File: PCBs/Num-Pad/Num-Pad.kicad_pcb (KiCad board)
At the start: 4 copper layers, 80 x 80 mm, 29 parts, among them J1 Male_Pogo_Connector_01x05, J2 Male_Pogo_Connector_01x05, J3 Male_Pogo_Connector_01x05, J4 Male_Pogo_Connector_01x05, SW1 SW_Push_45deg, SW10 SW_Push_45deg, SW11 SW_Push_45deg, SW12 SW_Push_45deg, SW2 SW_Push_45deg, SW3 SW_Push_45deg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

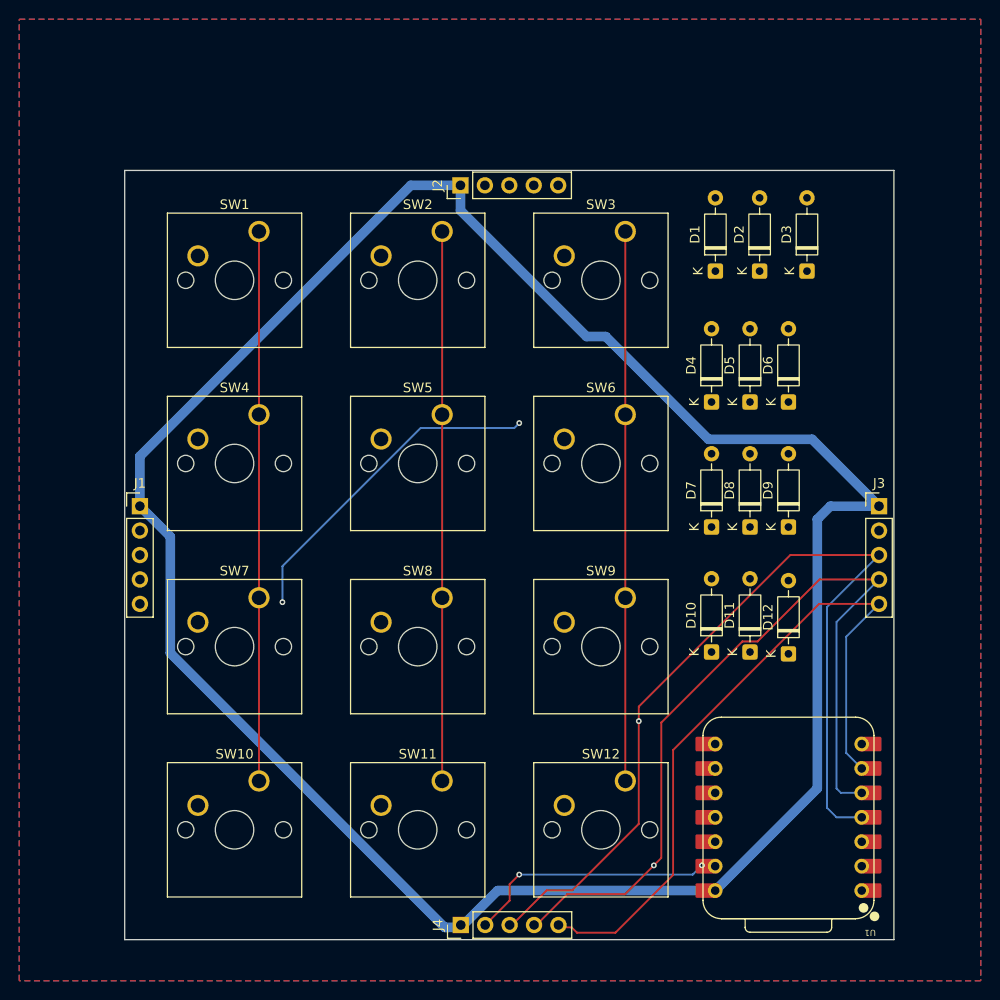
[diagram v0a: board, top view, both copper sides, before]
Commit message: Refactor I2C module handling and update PCB files
Major refactor of I2C communication between the main board and modules: unified pin naming, improved interrupt and keymap handling, and enhanced display logic in the main firmware. Updated PCB project files, added new production outputs (BOM, netlist, positions), and removed obsolete zipped PCB files. Hardware pin assignments and I2C protocol logic were aligned across modules for consistency and reliability.
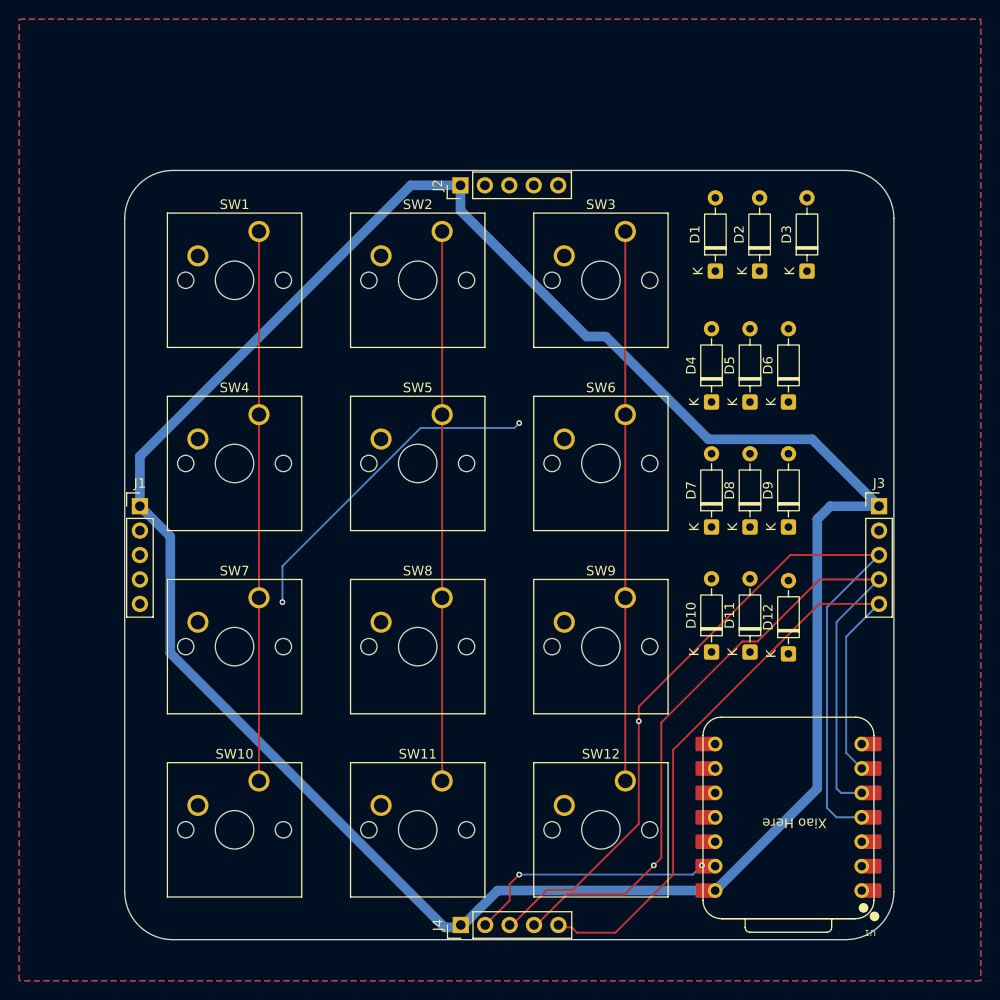
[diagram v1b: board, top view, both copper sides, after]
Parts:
- added G***: LOGO, LOGO, B.Cu at (149.0, 101.0)
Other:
- outline, holes or cut-outs redrawn
- board text added: "BeanPad NumPad Ginobeano V1"
- board text added: "Xiao Here"
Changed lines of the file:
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@@
 		)
 	)
-	(gr_rect
-		(start 90.96875 45.725)
-		(end 170.96875 125.725)
-		(stroke
-			(width 0.05)
-			(type default)
-		)
-		(fill no)
-		(layer "Edge.Cuts")
+	(footprint "LOGO"
+		(layer "B.Cu")
+		(at 149 101 -90)
+		(property "Reference" "G***"
+			(at 0 0 90)
+			(layer "B.SilkS")
+			(effects
+				(font
+					(size 1.5 1.5)
+					(thickness 0.3)
+				)
+				(justify mirror)
+			)
+		)
+		(property "Value" "LOGO"
+			(at 0.75 0 90)
+			(layer "B.SilkS")
+			(hide yes)
+			(effects
+				(font
+					(size 1.5 1.5)
+					(thickness 0.3)
+				)
+				(justify mirror)
+			)
+		)
+		(property "Datasheet" ""
+			(at 0 0 90)
+			(layer "B.Fab")
+			(hide yes)
+			(effects
+				(font
+					(size 1.27 1.27)
+					(thickness 0.15)
+				)
+				(justify mirror)
+			)
+		)
+		(property "Description" ""
+			(at 0 0 90)
+			(layer "B.Fab")
+			(hide yes)
+			(effects
+				(font
+					(size 1.27 1.27)
+					(thickness 0.15)
+				)
+				(justify mirror)
+			)
+		)
+		(attr board_only exclude_from_pos_files exclude_from_bom)
+		(fp_poly
+			(pts
+				(xy 11.286345 21.165835) (xy 12.614508 20.862313) (xy 13.919706 20.3992) (xy 14.604999 20.0848)
+				(xy 15.671747 19.467551) (xy 16.694462 18.70588) (xy 17.649618 17.823455) (xy 18.513686 16.84394)
+				(xy 19.26314 15.791001) (xy 19.781561 14.877713) (xy 20.051012 14.275829) (xy 20.312608 13.571256)
+				(xy 20.544686 12.830073) (xy 20.725577 12.11836) (xy 20.787079 11.811001) (xy 20.871597 11.202371)
+				(xy 20.933474 10.478661) (xy 20.971129 9.692812) (xy 20.98298 8.897763) (xy 20.967446 8.146453)
+				(xy 20.922945 7.491822) (xy 20.917637 7.441041) (xy 20.596928 5.255138) (xy 20.11204 3.090605) (xy 19.467729 0.957159)
+				(xy 18.668747 -1.135483) (xy 17.71985 -3.177601) (xy 16.62579 -5.159477) (xy 15.391323 -7.071394)
+				(xy 14.021202 -8.903632) (xy 12.520181 -10.646475) (xy 11.602011 -11.602011) (xy 9.89968 -13.193824)
+				(xy 8.119111 -14.640138) (xy 6.245781 -15.951425) (xy 4.265168 -17.138155) (xy 2.996851 -17.805998)
+				(xy 1.454155 -18.524908) (xy -0.131462 -19.161046) (xy -1.739936 -19.70995) (xy -3.351204 -20.167154)
+				(xy -4.945202 -20.528196) (xy -6.501868 -20.788612) (xy -8.001136 -20.943937) (xy -9.422944 -20.989707)
+				(xy -10.747228 -20.92146) (xy -10.922001 -20.902747) (xy -12.2785 -20.665051) (xy -13.577246 -20.274384)
+				(xy -14.808226 -19.740238) (xy -15.961426 -19.072106) (xy -17.026832 -18.279483) (xy -17.994431 -17.37186)
+				(xy -18.854209 -16.358731) (xy -19.596153 -15.249589) (xy -20.210248 -14.053927) (xy -20.686481 -12.781238)
+				(xy -21.014839 -11.441015) (xy -21.03754 -11.313075) (xy -21.109334 -10.73445) (xy -21.151212 -10.04694)
+				(xy -21.163235 -9.307275) (xy -21.145461 -8.572184) (xy -21.097948 -7.898397) (xy -21.033502 -7.412109)
+				(xy -20.712076 -6.052823) (xy -20.238633 -4.757898) (xy -19.621167 -3.538218) (xy -18.867669 -2.404666)
+				(xy -18.630293 -2.12555) (xy -11.836816 -2.12555) (xy -11.773225 -2.459418) (xy -11.600325 -2.741217)
+				(xy -11.342472 -2.937206) (xy -11.024018 -3.013647) (xy -10.879667 -3.002267) (xy -10.728455 -2.973726)
+				(xy -10.454763 -2.919952) (xy -10.102035 -2.849536) (xy -9.830964 -2.794864) (xy -8.242919 -2.394357)
+				(xy -6.72401 -1.853593) (xy -5.284087 -1.179782) (xy -3.933002 -0.380129) (xy -2.680605 0.538157)
+				(xy -1.53675 1.567869) (xy -0.511286 2.7018) (xy 0.385935 3.932742) (xy 1.130501 5.224669) (xy 1.364604 5.724203)
+				(xy 1.602663 6.298922) (xy 1.8344 6.916954) (xy 2.049536 7.546427) (xy 2.237793 8.155471) (xy 2.388893 8.712214)
+				(xy 2.492558 9.184784) (xy 2.53851 9.54131) (xy 2.53987 9.595014) (xy 2.463659 9.941543) (xy 2.257618 10.214342)
+				(xy 1.956087 10.379149) (xy 1.721012 10.412118) (xy 1.491512 10.395645) (xy 1.309705 10.334729)
+				(xy 1.160566 10.207617) (xy 1.029067 9.99256) (xy 0.900184 9.667806) (xy 0.758891 9.211605) (xy 0.667958 8.887746)
+				(xy 0.246002 7.544932) (xy -0.249744 6.334611) (xy -0.834741 5.230308) (xy -1.524449 4.205547) (xy -2.334329 3.233852)
+				(xy -3.071105 2.484572) (xy -4.145996 1.573064) (xy -5.343743 0.765661) (xy -6.647504 0.070772)
+				(xy -8.040434 -0.503196) (xy -9.50569 -0.947835) (xy -10.309716 -1.128952) (xy -10.810146 -1.232706)
+				(xy -11.170897 -1.321801) (xy -11.419483 -1.408405) (xy -11.583421 -1.504687) (xy -11.690224 -1.622818)
+				(xy -11.766743 -1.773352) (xy -11.836816 -2.12555) (xy -18.630293 -2.12555) (xy -17.986135 -1.368125)
+				(xy -16.984557 -0.439477) (xy -15.870929 0.370393) (xy -14.912958 0.921229) (xy -14.13295 1.283293)
+				(xy -13.303402 1.600306) (xy -12.482281 1.852547) (xy -11.727551 2.020296) (xy -11.641667 2.034203)
+				(xy -10.274556 2.323589) (xy -8.991877 2.758345) (xy -7.787782 3.341517) (xy -6.656424 4.076153)
+				(xy -5.591955 4.965297) (xy -5.117411 5.432968) (xy -4.212606 6.487665) (xy -3.454591 7.623224)
+				(xy -2.846881 8.832729) (xy -2.392992 10.109265) (xy -2.113263 11.34303) (xy -1.828175 12.691971)
+				(xy -1.442078 13.919352) (xy -0.943538 15.047312) (xy -0.321119 16.097992) (xy 0.436613 17.093535)
+				(xy 1.341094 18.05608) (xy 1.366463 18.080664) (xy 2.418697 18.98429) (xy 3.550111 19.743787) (xy 4.747936 20.357224)
+				(xy 5.999404 20.822666) (xy 7.291746 21.138181) (xy 8.612196 21.301836) (xy 9.947985 21.311698)
+			)
+			(stroke
+				(width 0)
+				(type solid)
+			)
+			(fill yes)
+			(layer "B.SilkS")
+		)
+		(embedded_fonts no)
+	)
+	(gr_line
+		(start 90.96875 120.725)
+		(end 90.96875 50.725)
+		(stroke
+			(width 0.05)
+			(type default)
+		)
+		(layer "Edge.Cuts")
+	)
+	(gr_arc
+		(start 170.96875 120.725)
+		(mid 169.504281 124.260516)
+		(end 165.96875 125.725)
+		(stroke
+			(width 0.05)
+			(type default)
+		)
+		(layer "Edge.Cuts")
+	)
+	(gr_arc
+		(start 165.96875 45.725)
+		(mid 169.504316 47.189448)
+		(end 170.96875 50.725)
+		(stroke
+			(width 0.05)
+			(type default)
+		)
+		(layer "Edge.Cuts")
+	)
+	(gr_line
+		(start 170.96875 50.725)
+		(end 170.96875 120.725)
+		(stroke
+			(width 0.05)
+			(type default)
+		)
+		(layer "Edge.Cuts")
+	)
+	(gr_arc
+		(start 90.96875 50.725)
+		(mid 92.433219 47.189484)
+		(end 95.96875 45.725)
+		(stroke
+			(width 0.05)
+			(type default)
+		)
+		(layer "Edge.Cuts")
+	)
+	(gr_line
+		(start 165.96875 125.725)
+		(end 95.96875 125.725)
+		(stroke
+			(width 0.05)
+			(type default)
+		)
+		(layer "Edge.Cuts")
+	)
+	(gr_line
+		(start 95.96875 45.725)
+		(end 165.96875 45.725)
+		(stroke
+			(width 0.05)
+			(type default)
+		)
+		(layer "Edge.Cuts")
+	)
+	(gr_arc
+		(start 95.96875 125.725)
+		(mid 92.433216 124.260534)
+		(end 90.96875 120.725)
+		(stroke
+			(width 0.05)
+			(type default)
+		)
+		(layer "Edge.Cuts")
+	)
+	(gr_text "Xiao Here\n"
+		(at 164 113 180)
+		(layer "F.SilkS")
+		(effects
+			(font
+				(size 1 1)
+				(thickness 0.1)
+			)
+			(justify left bottom)
+		)
+	)
+	(gr_text "BeanPad\nNumPad\nGinobeano\nV1"
+		(at 135 83 0)
+		(layer "B.SilkS")
+		(effects
+			(font
+				(size 5 5)
+				(thickness 0.625)
+			)
+			(justify left bottom mirror)
+		)
 	)
 	(segment
